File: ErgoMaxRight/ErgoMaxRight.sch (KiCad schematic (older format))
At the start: 92 parts, among them J1 PJ-320A, K1 KEYSW, K10 KEYSW, K11 KEYSW, K12 KEYSW, K13 KEYSW, K14 KEYSW, K15 KEYSW, K16 KEYSW, K17 KEYSW, K18 KEYSW, K19 KEYSW, K2 KEYSW, K20 KEYSW, K21 KEYSW, K22 KEYSW, K23 KEYSW, K24 KEYSW, K25 KEYSW, K26 KEYSW, K27 KEYSW, K28 KEYSW, K29 KEYSW, K3 KEYSW, K30 KEYSW, K31 KEYSW, K32 KEYSW, K33 KEYSW, K34 KEYSW, K35 KEYSW, K36 KEYSW, K37 KEYSW, K38 KEYSW, K39 KEYSW, K4 KEYSW, K40 KEYSW, K41 KEYSW, K42 KEYSW, K43 KEYSW, K44 KEYSW, K5 KEYSW, K6 KEYSW, K7 KEYSW, K8 KEYSW, K9 KEYSW, U1 ProMicro

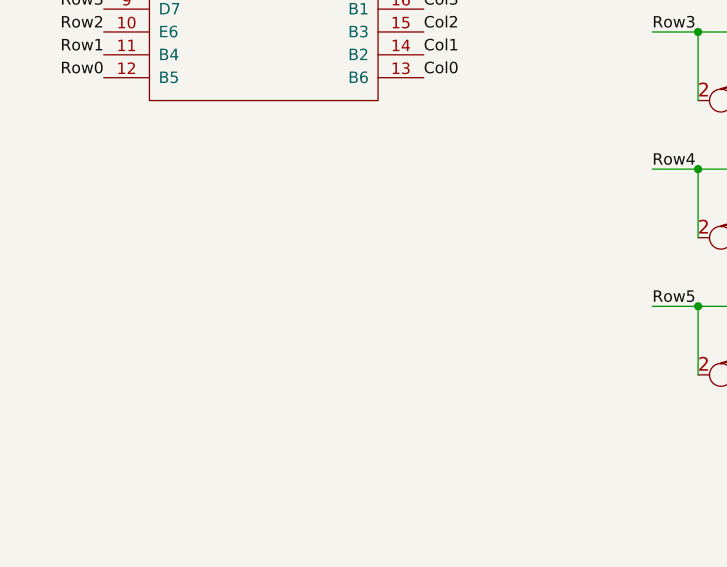
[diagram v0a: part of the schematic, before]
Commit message: modify library for MX Kailh sockets; add mounting holes in schema for PCB
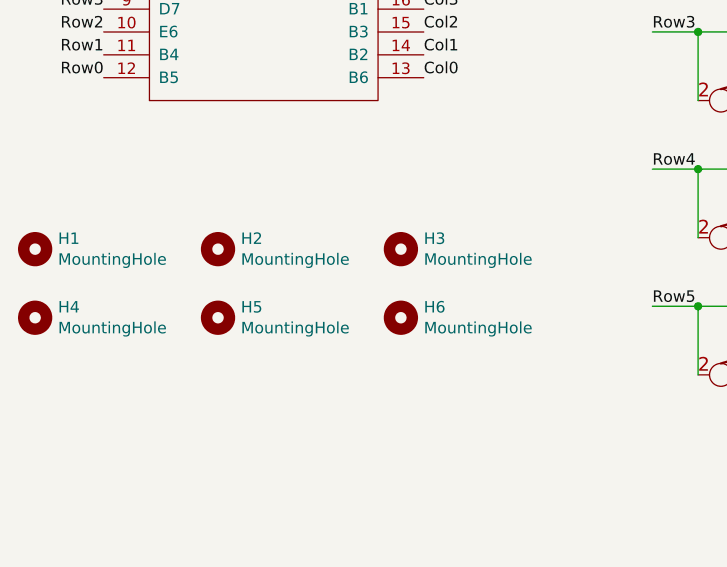
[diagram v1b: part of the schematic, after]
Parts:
- added H1, H2, H3, H4, H5, H6: MountingHole, MountingHole:MountingHole_6mm, symbol Mechanical:MountingHole
- K1, K10, K11, K12, K13, K14, K15, K16, K17, K18, K19, K2, K20, K21, K22, K23, K24, K25, K26, K27, K28, K29, K3, K30, K31, K32, K33, K34, K35, K36, K37, K38, K39, K4, K40, K41, K42, K43, K44, K5, K6, K7, K8, K9: footprint keyboard_parts:Kailh_MX_Socket -> Kailh_MX_socket:Kailh_MX_Socket

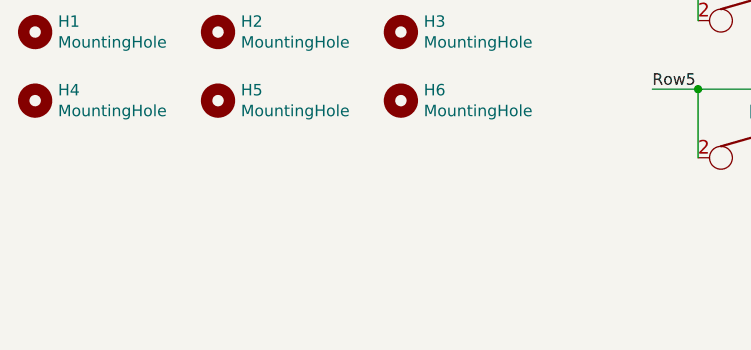
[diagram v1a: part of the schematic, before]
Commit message: add missing stabs in schema, add them back in PCB
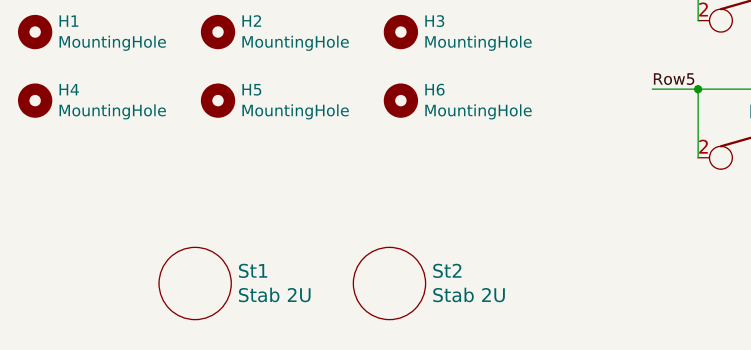
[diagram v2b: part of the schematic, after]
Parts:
- added St1, St2: Stab 2U, keyboard_parts:Mx_Stab_200, symbol keebio:Hole
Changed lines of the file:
@@
+	1    0    0    -1
+$EndComp
+$Comp
+L keebio:Hole St1
+U 1 1 5BF6492E
+P 1650 5600
+F 0 "St1" H 1836 5653 60  0000 L CNN
+F 1 "Stab 2U" H 1836 5547 60  0000 L CNN
+F 2 "keyboard_parts:Mx_Stab_200" H 1650 5600 60  0001 C CNN
+F 3 "" H 1650 5600 60  0001 C CNN
+	1    1650 5600
+	1    0    0    -1
+$EndComp
+$Comp
+L keebio:Hole St2
+U 1 1 5BF64AA9
+P 2500 5600
+F 0 "St2" H 2686 5653 60  0000 L CNN
+F 1 "Stab 2U" H 2686 5547 60  0000 L CNN
+F 2 "keyboard_parts:Mx_Stab_200" H 2500 5600 60  0001 C CNN
+F 3 "" H 2500 5600 60  0001 C CNN
+	1    2500 5600
 	1    0    0    -1
 $EndComp

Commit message: rename footprint library to ErgoMax for clarity
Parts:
- K1, K10, K11, K12, K13, K14, K15, K16, K17, K18, K19, K2, K20, K21, K22, K23, K24, K25, K26, K27, K28, K29, K3, K30, K31, K32, K33, K34, K35, K36, K37, K38, K39, K4, K40, K41, K42, K43, K44, K5, K6, K7, K8, K9: footprint Kailh_MX_socket:Kailh_MX_Socket -> ErgoMax:Kailh_MX_Socket

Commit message: add custom logos in schema and PCB (added them in libs)
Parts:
- added Lg1: Logo, ErgoMax:LouWii-logo, symbol ErgoMax:Logo
- added Lg2: Logo, ErgoMax:ErgoMax-logo, symbol ErgoMax:Logo
- St1, St2: symbol keebio:Hole -> ErgoMax:Stabilizer
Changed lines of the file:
@@
 $EndComp
 $Comp
-L keebio:Hole St1
+L ErgoMax:Stabilizer St1
 U 1 1 5BF6492E
 P 1650 5600
@@
 $EndComp
 $Comp
-L keebio:Hole St2
+L ErgoMax:Stabilizer St2
 U 1 1 5BF64AA9
 P 2500 5600
@@
 	1    0    0    -1
 $EndComp
+$Comp
+L ErgoMax:Logo Lg1
+U 1 1 5BF4E224
+P 1650 6000
+F 0 "Lg1" H 1778 6046 50  0000 L CNN
+F 1 "Logo" H 1778 5955 50  0000 L CNN
+F 2 "ErgoMax:LouWii-logo" H 1650 5900 50  0001 C CNN
+F 3 "" H 1650 5900 50  0001 C CNN
+	1    1650 6000
+	1    0    0    -1
+$EndComp
+$Comp
+L ErgoMax:Logo Lg2
+U 1 1 5BF4E344
+P 2500 6000
+F 0 "Lg2" H 2628 6046 50  0000 L CNN
+F 1 "Logo" H 2628 5955 50  0000 L CNN
+F 2 "ErgoMax:ErgoMax-logo" H 2500 5900 50  0001 C CNN
+F 3 "" H 2500 5900 50  0001 C CNN
+	1    2500 6000
+	1    0    0    -1
+$EndComp

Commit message: add add values for main keys on PCB
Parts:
- K1: value KEYSW -> F12
- K10: value KEYSW -> 8 *
- K11: value KEYSW -> 7 &
- K12: value KEYSW -> 6 ^
- K15: value KEYSW -> P
- K16: value KEYSW -> O
- K17: value KEYSW -> I
- K18: value KEYSW -> U
- K19: value KEYSW -> Y
- K2: value KEYSW -> F11
- K22: value KEYSW -> ; :
- K23: value KEYSW -> L
- K24: value KEYSW -> K
- K25: value KEYSW -> J
- K26: value KEYSW -> H
- K3: value KEYSW -> F10
- K30: value KEYSW -> / ?
- K31: value KEYSW -> . >
- K32: value KEYSW -> , <
- K33: value KEYSW -> M
- K34: value KEYSW -> N
- K4: value KEYSW -> F9
- K5: value KEYSW -> F8
- K6: value KEYSW -> F7
- K8: value KEYSW -> 0 )
- K9: value KEYSW -> 9 (
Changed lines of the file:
@@
 P 5000 2050
 F 0 "K1" H 5000 2283 60  0000 C CNN
-F 1 "KEYSW" H 5000 1950 60  0001 C CNN
+F 1 "F12" H 5000 1950 60  0001 C CNN
 F 2 "ErgoMax:Kailh_MX_Socket" H 5000 2050 60  0001 C CNN
 F 3 "" H 5000 2050 60  0000 C CNN
@@
 P 5850 2050
 F 0 "K2" H 5850 2283 60  0000 C CNN
-F 1 "KEYSW" H 5850 1950 60  0001 C CNN
+F 1 "F11" H 5850 1950 60  0001 C CNN
 F 2 "ErgoMax:Kailh_MX_Socket" H 5850 2050 60  0001 C CNN
 F 3 "" H 5850 2050 60  0000 C CNN
@@
 P 6700 2050
 F 0 "K3" H 6700 2283 60  0000 C CNN
-F 1 "KEYSW" H 6700 1950 60  0001 C CNN
+F 1 "F10" H 6700 1950 60  0001 C CNN
 F 2 "ErgoMax:Kailh_MX_Socket" H 6700 2050 60  0001 C CNN
 F 3 "" H 6700 2050 60  0000 C CNN
@@
 P 7550 2050
 F 0 "K4" H 7550 2283 60  0000 C CNN
-F 1 "KEYSW" H 7550 1950 60  0001 C CNN
+F 1 "F9" H 7550 1950 60  0001 C CNN
 F 2 "ErgoMax:Kailh_MX_Socket" H 7550 2050 60  0001 C CNN
 F 3 "" H 7550 2050 60  0000 C CNN
@@
 P 8400 2050
 F 0 "K5" H 8400 2283 60  0000 C CNN
-F 1 "KEYSW" H 8400 1950 60  0001 C CNN
+F 1 "F8" H 8400 1950 60  0001 C CNN
 F 2 "ErgoMax:Kailh_MX_Socket" H 8400 2050 60  0001 C CNN
 F 3 "" H 8400 2050 60  0000 C CNN
@@
 P 9250 2050
 F 0 "K6" H 9250 2283 60  0000 C CNN
-F 1 "KEYSW" H 9250 1950 60  0001 C CNN
+F 1 "F7" H 9250 1950 60  0001 C CNN
 F 2 "ErgoMax:Kailh_MX_Socket" H 9250 2050 60  0001 C CNN
 F 3 "" H 9250 2050 60  0000 C CNN
@@
 P 5000 2650
 F 0 "K8" H 5000 2850 60  0000 C CNN
-F 1 "KEYSW" H 5000 2550 60  0001 C CNN
+F 1 "0 )" H 5000 2550 60  0001 C CNN
 F 2 "ErgoMax:Kailh_MX_Socket" H 5000 2650 60  0001 C CNN
 F 3 "" H 5000 2650 60  0000 C CNN
@@
 P 5850 2650
 F 0 "K9" H 5850 2850 60  0000 C CNN
-F 1 "KEYSW" H 5850 2550 60  0001 C CNN
+F 1 "9 (" H 5850 2550 60  0001 C CNN
 F 2 "ErgoMax:Kailh_MX_Socket" H 5850 2650 60  0001 C CNN
 F 3 "" H 5850 2650 60  0000 C CNN
@@
 P 6700 2650
 F 0 "K10" H 6700 2850 60  0000 C CNN
-F 1 "KEYSW" H 6700 2550 60  0001 C CNN
+F 1 "8 *" H 6700 2550 60  0001 C CNN
 F 2 "ErgoMax:Kailh_MX_Socket" H 6700 2650 60  0001 C CNN
 F 3 "" H 6700 2650 60  0000 C CNN
@@
 P 7550 2650
 F 0 "K11" H 7550 2850 60  0000 C CNN
-F 1 "KEYSW" H 7550 2550 60  0001 C CNN
+F 1 "7 &" H 7550 2550 60  0001 C CNN
 F 2 "ErgoMax:Kailh_MX_Socket" H 7550 2650 60  0001 C CNN
 F 3 "" H 7550 2650 60  0000 C CNN
@@
 P 8400 2650
 F 0 "K12" H 8400 2850 60  0000 C CNN
-F 1 "KEYSW" H 8400 2550 60  0001 C CNN
+F 1 "6 ^" H 8400 2550 60  0001 C CNN
 F 2 "ErgoMax:Kailh_MX_Socket" H 8400 2650 60  0001 C CNN
 F 3 "" H 8400 2650 60  0000 C CNN
@@
 P 5000 3250
 F 0 "K15" H 5000 3450 60  0000 C CNN
-F 1 "KEYSW" H 5000 3150 60  0001 C CNN
+F 1 "P" H 5000 3150 60  0001 C CNN
 F 2 "ErgoMax:Kailh_MX_Socket" H 5000 3250 60  0001 C CNN
 F 3 "" H 5000 3250 60  0000 C CNN
@@
 P 5850 3250
 F 0 "K16" H 5850 3450 60  0000 C CNN
-F 1 "KEYSW" H 5850 3150 60  0001 C CNN
+F 1 "O" H 5850 3150 60  0001 C CNN
 F 2 "ErgoMax:Kailh_MX_Socket" H 5850 3250 60  0001 C CNN
 F 3 "" H 5850 3250 60  0000 C CNN
@@
 P 6700 3250
 F 0 "K17" H 6700 3450 60  0000 C CNN
-F 1 "KEYSW" H 6700 3150 60  0001 C CNN
+F 1 "I" H 6700 3150 60  0001 C CNN
 F 2 "ErgoMax:Kailh_MX_Socket" H 6700 3250 60  0001 C CNN
 F 3 "" H 6700 3250 60  0000 C CNN
@@
 P 7550 3250
 F 0 "K18" H 7550 3450 60  0000 C CNN
-F 1 "KEYSW" H 7550 3150 60  0001 C CNN
+F 1 "U" H 7550 3150 60  0001 C CNN
 F 2 "ErgoMax:Kailh_MX_Socket" H 7550 3250 60  0001 C CNN
 F 3 "" H 7550 3250 60  0000 C CNN
@@
 P 8400 3250
 F 0 "K19" H 8400 3450 60  0000 C CNN
-F 1 "KEYSW" H 8400 3150 60  0001 C CNN
+F 1 "Y" H 8400 3150 60  0001 C CNN
 F 2 "ErgoMax:Kailh_MX_Socket" H 8400 3250 60  0001 C CNN
 F 3 "" H 8400 3250 60  0000 C CNN
@@
 P 5000 3850
 F 0 "K22" H 5000 4050 60  0000 C CNN
-F 1 "KEYSW" H 5000 3750 60  0001 C CNN
+F 1 "; :" H 5000 3750 60  0001 C CNN
 F 2 "ErgoMax:Kailh_MX_Socket" H 5000 3850 60  0001 C CNN
 F 3 "" H 5000 3850 60  0000 C CNN
@@
 P 5850 3850
 F 0 "K23" H 5850 4050 60  0000 C CNN
-F 1 "KEYSW" H 5850 3750 60  0001 C CNN
+F 1 "L" H 5850 3750 60  0001 C CNN
 F 2 "ErgoMax:Kailh_MX_Socket" H 5850 3850 60  0001 C CNN
 F 3 "" H 5850 3850 60  0000 C CNN
@@
 P 6700 3850
 F 0 "K24" H 6700 4050 60  0000 C CNN
-F 1 "KEYSW" H 6700 3750 60  0001 C CNN
+F 1 "K" H 6700 3750 60  0001 C CNN
 F 2 "ErgoMax:Kailh_MX_Socket" H 6700 3850 60  0001 C CNN
 F 3 "" H 6700 3850 60  0000 C CNN
@@
 P 7550 3850
 F 0 "K25" H 7550 4050 60  0000 C CNN
-F 1 "KEYSW" H 7550 3750 60  0001 C CNN
+F 1 "J" H 7550 3750 60  0001 C CNN
 F 2 "ErgoMax:Kailh_MX_Socket" H 7550 3850 60  0001 C CNN
 F 3 "" H 7550 3850 60  0000 C CNN
@@
 P 8400 3850
 F 0 "K26" H 8400 4050 60  0000 C CNN
-F 1 "KEYSW" H 8400 3750 60  0001 C CNN
+F 1 "H" H 8400 3750 60  0001 C CNN
 F 2 "ErgoMax:Kailh_MX_Socket" H 8400 3850 60  0001 C CNN
 F 3 "" H 8400 3850 60  0000 C CNN
@@
 P 5000 4450
 F 0 "K30" H 5000 4650 60  0000 C CNN
-F 1 "KEYSW" H 5000 4350 60  0001 C CNN
+F 1 "/ ?" H 5000 4350 60  0001 C CNN
 F 2 "ErgoMax:Kailh_MX_Socket" H 5000 4450 60  0001 C CNN
 F 3 "" H 5000 4450 60  0000 C CNN
@@
 P 5850 4450
 F 0 "K31" H 5850 4650 60  0000 C CNN
-F 1 "KEYSW" H 5850 4350 60  0001 C CNN
+F 1 ". >" H 5850 4350 60  0001 C CNN
 F 2 "ErgoMax:Kailh_MX_Socket" H 5850 4450 60  0001 C CNN
 F 3 "" H 5850 4450 60  0000 C CNN
@@
 P 6700 4450
 F 0 "K32" H 6700 4650 60  0000 C CNN
-F 1 "KEYSW" H 6700 4350 60  0001 C CNN
+F 1 ", <" H 6700 4350 60  0001 C CNN
 F 2 "ErgoMax:Kailh_MX_Socket" H 6700 4450 60  0001 C CNN
 F 3 "" H 6700 4450 60  0000 C CNN
@@
 P 7550 4450
 F 0 "K33" H 7550 4650 60  0000 C CNN
-F 1 "KEYSW" H 7550 4350 60  0001 C CNN
+F 1 "M" H 7550 4350 60  0001 C CNN
 F 2 "ErgoMax:Kailh_MX_Socket" H 7550 4450 60  0001 C CNN
 F 3 "" H 7550 4450 60  0000 C CNN
@@
 P 8400 4450
 F 0 "K34" H 8400 4650 60  0000 C CNN
-F 1 "KEYSW" H 8400 4350 60  0001 C CNN
+F 1 "N" H 8400 4350 60  0001 C CNN
 F 2 "ErgoMax:Kailh_MX_Socket" H 8400 4450 60  0001 C CNN
 F 3 "" H 8400 4450 60  0000 C CNN

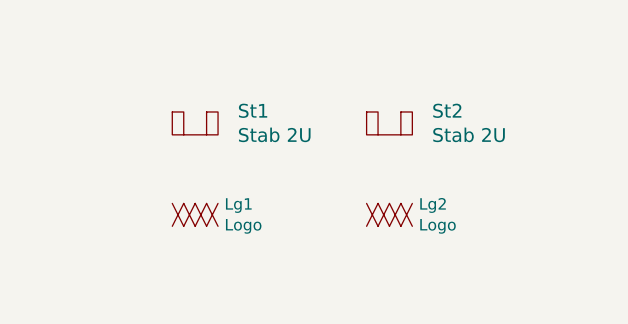
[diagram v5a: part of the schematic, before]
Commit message: move logos to front side of left and right PCB, add left/right writings
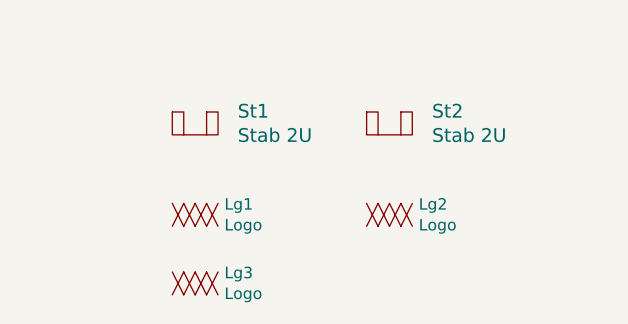
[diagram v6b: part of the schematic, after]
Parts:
- added Lg3: Logo, ErgoMax:RightSideText, symbol ErgoMax:Logo
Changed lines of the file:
@@
+	1    0    0    -1
+$EndComp
+$Comp
+L ErgoMax:Logo Lg3
+U 1 1 5C032B7F
+P 1650 6300
+F 0 "Lg3" H 1778 6346 50  0000 L CNN
+F 1 "Logo" H 1778 6255 50  0000 L CNN
+F 2 "ErgoMax:RightSideText" H 1650 6200 50  0001 C CNN
+F 3 "" H 1650 6200 50  0001 C CNN
+	1    1650 6300
 	1    0    0    -1
 $EndComp
